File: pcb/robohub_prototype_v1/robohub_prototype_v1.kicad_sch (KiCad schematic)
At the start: 0 parts

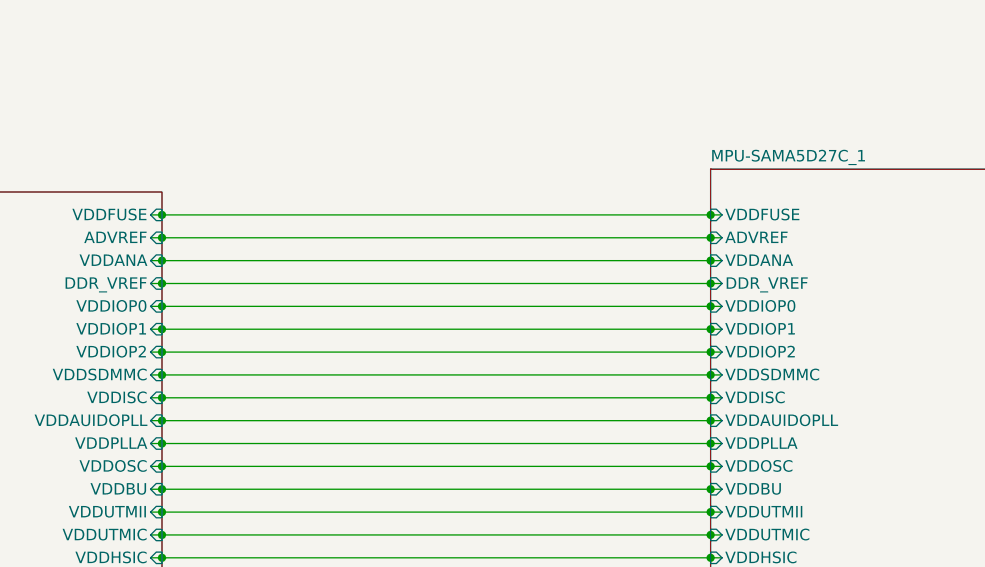
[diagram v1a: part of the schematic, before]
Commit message: Start routing ddr2
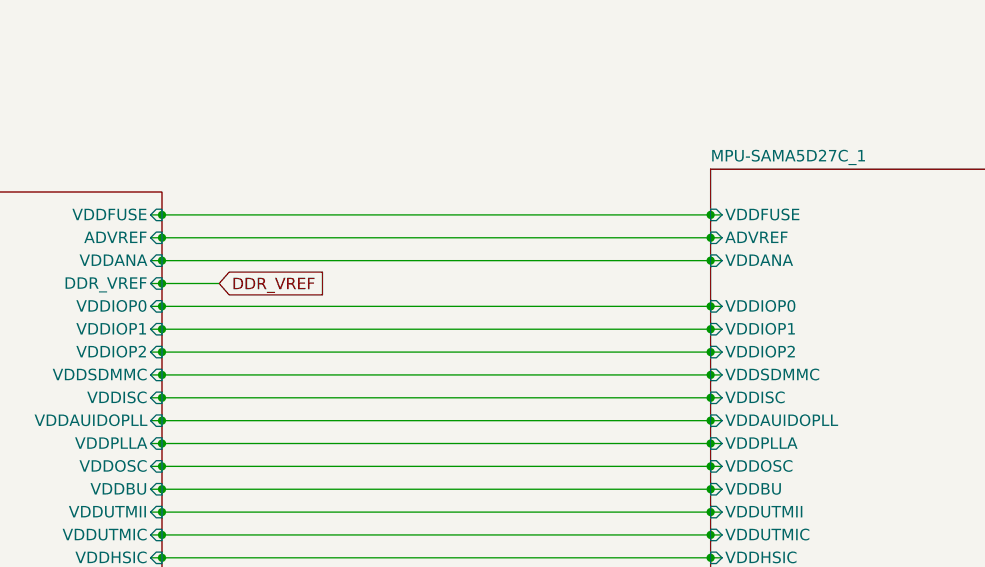
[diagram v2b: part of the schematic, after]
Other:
- sheet MPU-SAMA5D27C_1 ports: added none; removed DDR_VREF
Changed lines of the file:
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@@
-	)
-	(junction
-		(at 166.37 85.09)
-		(diameter 0)
-		(color 0 0 0 0)
 	)
 	(junction
@@
 	)
 	(junction
+		(at 105.41 85.09)
+		(diameter 0)
+		(color 0 0 0 0)
+	)
+	(junction
 		(at 105.41 105.41)
 		(diameter 0)
@@
 	)
 	(junction
-		(at 105.41 85.09)
-		(diameter 0)
-		(color 0 0 0 0)
-	)
-	(junction
 		(at 166.37 100.33)
 		(diameter 0)
@@
 	(wire
 		(pts
-			(xy 166.37 85.09) (xy 167.64 85.09)
-		)
-		(stroke
-			(width 0)
-			(type default)
-		)
-	)
-	(wire
-		(pts
 			(xy 166.37 87.63) (xy 167.64 87.63)
 		)
@@
 	(wire
 		(pts
+			(xy 105.41 85.09) (xy 111.76 85.09)
+		)
+		(stroke
+			(width 0)
+			(type default)
+		)
+	)
+	(wire
+		(pts
 			(xy 104.14 77.47) (xy 105.41 77.47)
 		)
@@
 		(pts
 			(xy 105.41 100.33) (xy 166.37 100.33)
-		)
-		(stroke
-			(width 0)
-			(type default)
-		)
-	)
-	(wire
-		(pts
-			(xy 105.41 85.09) (xy 166.37 85.09)
 		)
 		(stroke
@@
 				)
 				(justify right)
+				(hide yes)
+			)
+		)
+	)
+	(global_label "DDR_VREF"
+		(shape input)
+		(at 111.76 85.09 0)
+		(fields_autoplaced yes)
+		(effects
+			(font
+				(size 1.27 1.27)
+			)
+			(justify left)
+		)
+		(property "Intersheetrefs" "${INTERSHEET_REFS}"
+			(at 124.119 85.09 0)
+			(effects
+				(font
+					(size 1.27 1.27)
+				)
+				(justify left)
 				(hide yes)
 			)
@@
 			(effects
 				(font
-					(size 1.27 1.27)
-				)
-				(justify left)
-			)
-		)
-		(pin "DDR_VREF" input
-			(at 166.37 85.09 180)
-			(effects
-				(font
